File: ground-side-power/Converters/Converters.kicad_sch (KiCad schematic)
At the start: 31 parts, among them J10 Conn_01x03_Female, J12 Conn_01x04_Female, J13 DAQ Voltage Sensing, J14 DAQ Current Sensing, J27 Conn_01x02_Female, U3 K7805-3AR3, U4 INA180, U5 INA180, U6 URB2424LD-20WR3

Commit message: resolved issues from testing
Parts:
- added J11: Ground Connections, GSP:1935310, symbol Connector:Screw_Terminal_01x02
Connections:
- net GND: now also U6.6 (0V), J11.1 (Pin_1), J11.2 (Pin_2); no longer U6.5 (0V)
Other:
- moved on the sheet: C15

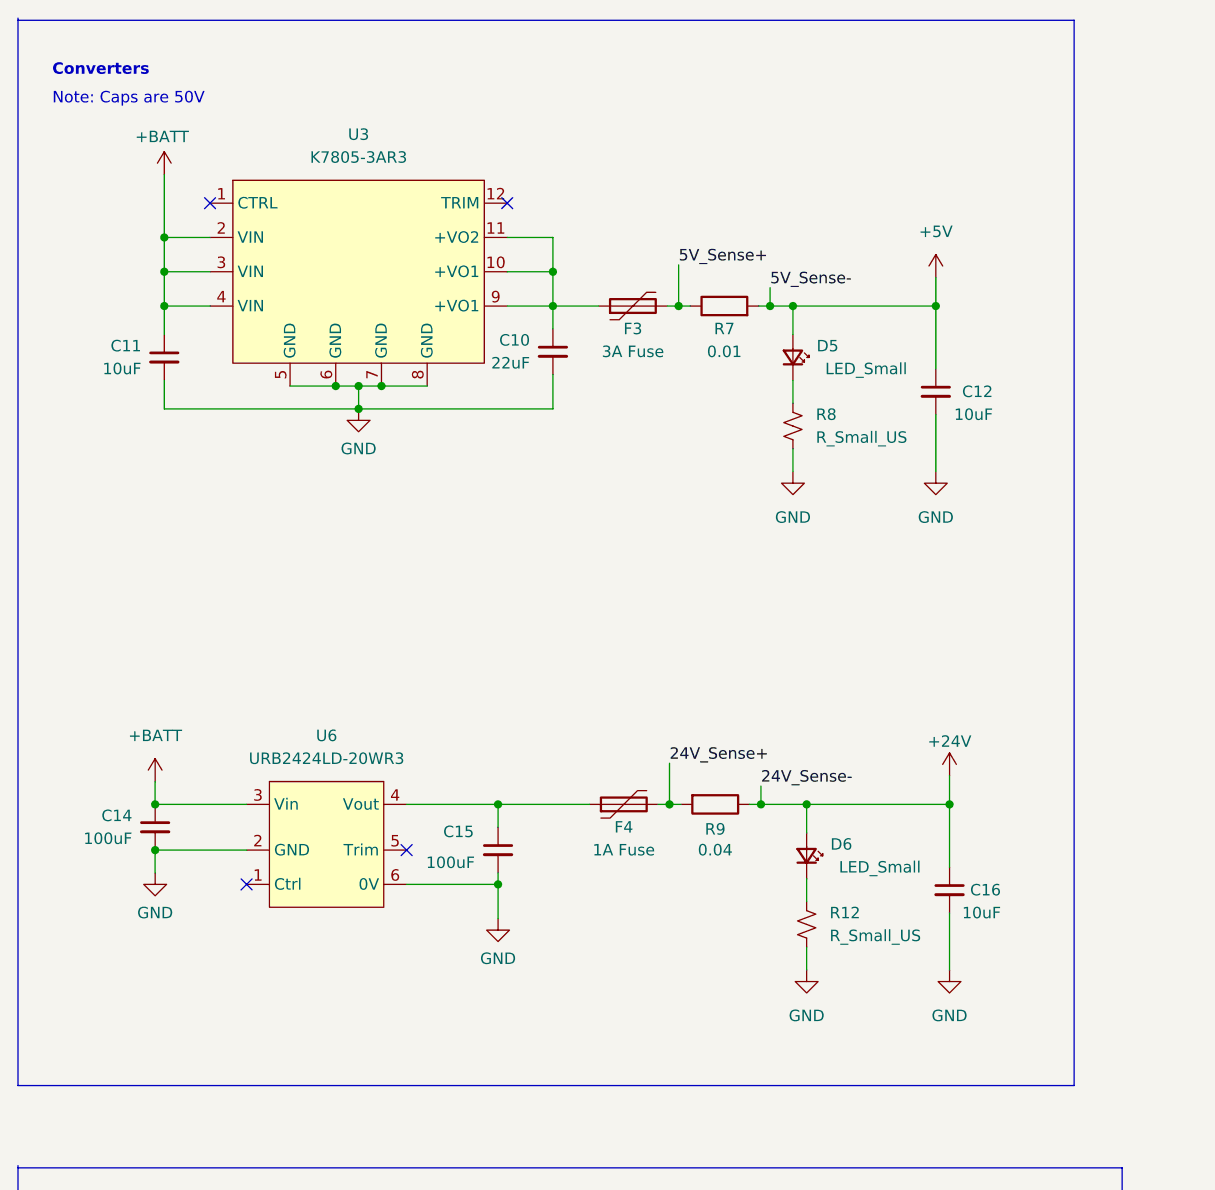
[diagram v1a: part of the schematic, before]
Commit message: schematic for new converter
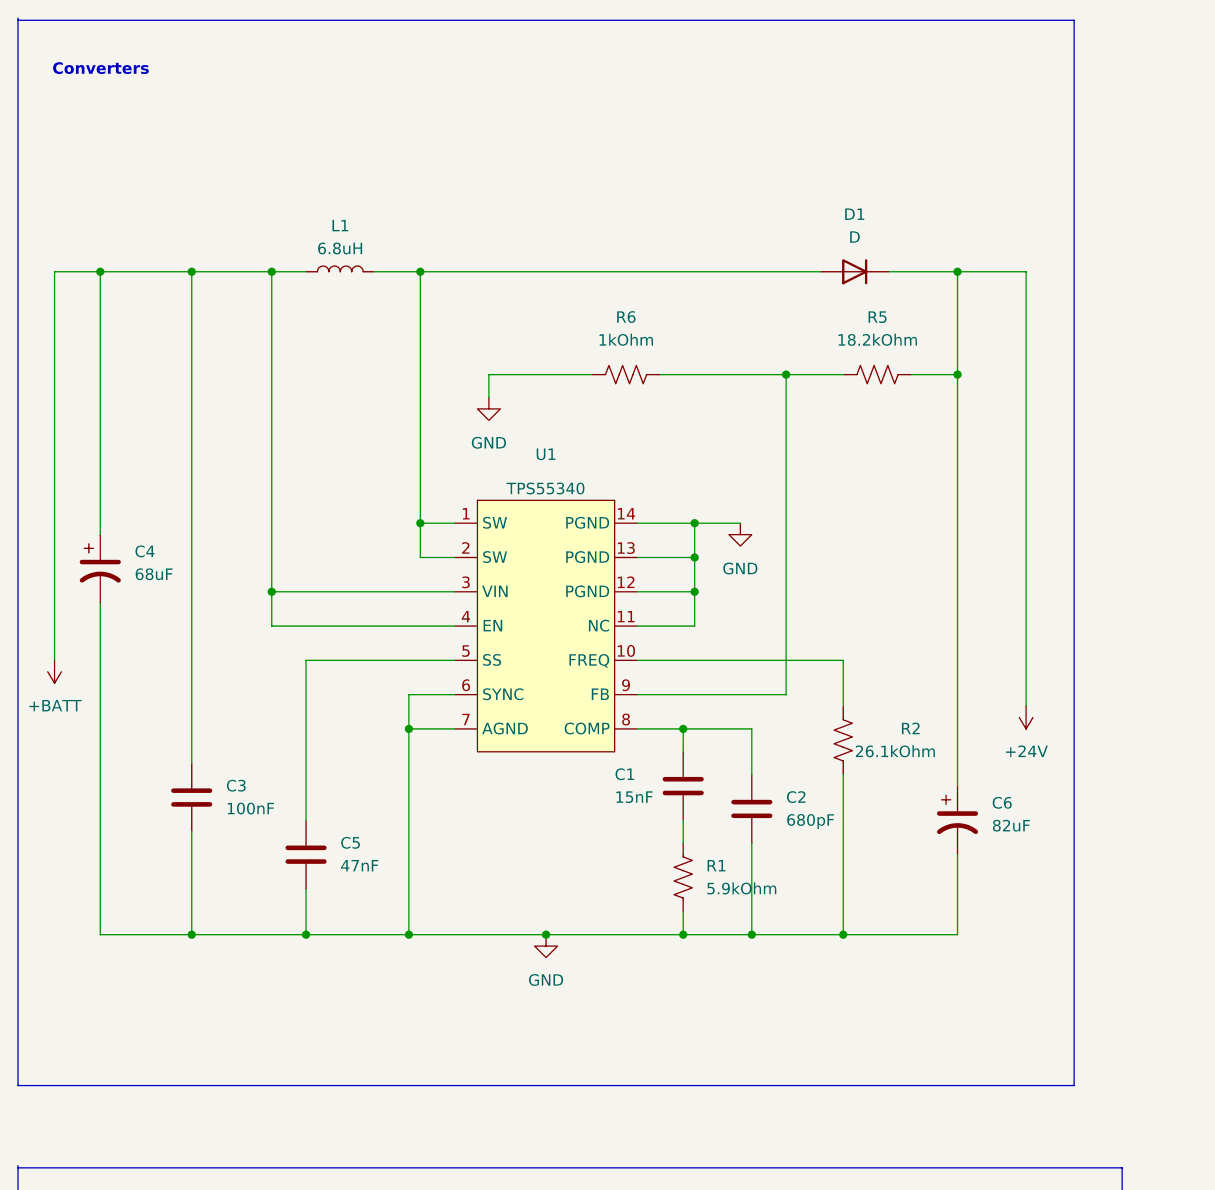
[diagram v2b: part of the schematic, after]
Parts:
- removed C10: 22uF, Capacitor_SMD:C_0805_2012Metric_Pad1.18x1.45mm_HandSolder, symbol Device:C_Small
- removed C11, C12, C16: 10uF, Capacitor_SMD:C_0805_2012Metric_Pad1.18x1.45mm_HandSolder, symbol Device:C_Small
- removed C14, C15: 100uF, Capacitor_THT:CP_Radial_D6.3mm_P2.50mm, symbol Device:C_Small
- removed D5, D6: LED_Small, Diode_SMD:D_1206_3216Metric_Pad1.42x1.75mm_HandSolder, symbol Device:LED_Small
- removed F3: 3A Fuse, Fuse:Fuseholder_Clip-6.3x32mm_Littelfuse_102_122_Inline_P34.21x7.62mm_D1.98mm_Horizontal, symbol Device:Polyfuse
- removed F4: 1A Fuse, Fuse:Fuseholder_Clip-6.3x32mm_Littelfuse_102_122_Inline_P34.21x7.62mm_D1.98mm_Horizontal, symbol Device:Polyfuse
- removed R12, R8: R_Small_US, Resistor_SMD:R_0805_2012Metric_Pad1.20x1.40mm_HandSolder, symbol Device:R_Small_US
- removed R7: 0.01, Resistor_SMD:R_2512_6332Metric_Pad1.40x3.35mm_HandSolder, symbol Device:R
- removed R9: 0.04, Resistor_SMD:R_2512_6332Metric_Pad1.40x3.35mm_HandSolder, symbol Device:R
- removed U3: K7805-3AR3, GSP:K7805-3AR3, symbol Regulator_Switching:AP63203WU
- removed U6: URB2424LD-20WR3, GSP:URB2424LD-20WR3, symbol GSP:URB2424LD-30WR3
- added C1: 15nF, Capacitor_SMD:C_0402_1005Metric_Pad0.74x0.62mm_HandSolder, symbol Device:C
- added C2: 680pF, Capacitor_SMD:C_0402_1005Metric_Pad0.74x0.62mm_HandSolder, symbol Device:C
- added C3: 100nF, Capacitor_SMD:C_0805_2012Metric_Pad1.18x1.45mm_HandSolder, symbol Device:C
- added C4: 68uF, Capacitor_SMD:C_Elec_6.3x7.7, symbol Device:C_Polarized_US
- added C5: 47nF, Capacitor_SMD:C_0201_0603Metric_Pad0.64x0.40mm_HandSolder, symbol Device:C
- added C6: 82uF, Capacitor_SMD:CP_Elec_8x11.9, symbol Device:C_Polarized_US
- added D1: D, Diode_SMD:D_SMB-SMC_Universal_Handsoldering, symbol Device:D
- added L1: 6.8uH, Inductor_SMD:L_Coilcraft_XAL6060-XXX, symbol Device:L
- added R1: 5.9kOhm, Resistor_SMD:R_0402_1005Metric_Pad0.72x0.64mm_HandSolder, symbol Device:R_US
- added R2: 26.1kOhm, Resistor_SMD:R_0402_1005Metric_Pad0.72x0.64mm_HandSolder, symbol Device:R_US
- added R5: 18.2kOhm, Resistor_SMD:R_0402_1005Metric_Pad0.72x0.64mm_HandSolder, symbol Device:R_US
- added R6: 1kOhm, Resistor_SMD:R_0402_1005Metric_Pad0.72x0.64mm_HandSolder, symbol Device:R_US
- added U1: TPS55340, Package_SO:TSSOP-14_4.4x3.6mm_P0.4mm, symbol Converter_Library:TPS55340
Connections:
- net +24V: now also C6.1, D1.1 (K), R5.2; no longer U5.4 (IN-)
- net +5V: no longer U4.4 (IN-)
- net +BATT: now also C3.1, C4.1, L1.1, U1.3 (VIN), U1.4 (EN)
- net GND: now also C2.2, C3.2, C4.2, C5.2, C6.2, R1.2, R2.2, R6.1, U1.11 (NC), U1.12 (PGND), U1.13 (PGND), U1.14 (PGND), U1.6 (SYNC), U1.7 (AGND)
- new net: R5.1, R6.2, U1.9 (FB)
- new net: C1.1, C2.1, U1.8 (COMP)
- new net: C1.2, R1.1
- new net: D1.2 (A), L1.2, U1.1 (SW), U1.2 (SW)
- new net: R2.1, U1.10 (FREQ)
- new net: C5.1, U1.5 (SS)
- new net 24V_Sense-: U5.4 (IN-)
- new net 5V_Sense-: U4.4 (IN-)
- no-connect marks 4 -> 0
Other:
- note removed: "Note: Caps are 50V"
- company: (none) -> Waterloo Rocketry
